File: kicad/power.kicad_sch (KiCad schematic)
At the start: 48 parts, among them J5 Conn_Coaxial_Power, J6 Screw_Terminal_01x02, U11 ADP7118ACPZN, U22 ADP7118ACPZN, U23 LTM8074EY-PBF, U7 LTM8078EY-PBF, U8 ADP7118ACPZN, U9 ADP7118ACPZN

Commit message: assign footprints
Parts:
- C15, C69, C7: footprint (none) -> Capacitor_SMD:C_0805_2012Metric_Pad1.18x1.45mm_HandSolder
- C16, C17, C18, C19, C20, C21, C26, C27, C28, C65, C66, C67, C68, C70, C71, C72, C8: footprint (none) -> Capacitor_SMD:C_0603_1608Metric_Pad1.08x0.95mm_HandSolder
- F1: footprint (none) -> Fuse:Fuse_2920_7451Metric_Pad2.10x5.45mm_HandSolder
- J5: footprint (none) -> Connector_BarrelJack:BarrelJack_CUI_PJ-063AH_Horizontal
- J6: footprint (none) -> TerminalBlock_Phoenix:TerminalBlock_Phoenix_MKDS-1,5-2_1x02_P5.00mm_Horizontal
- R12, R19, R21, R22, R65, R66, R67, R68, R69, R70, R71, R72, R73, R74, R75, R76, R77, R91, R92: footprint (none) -> Resistor_SMD:R_0603_1608Metric_Pad0.98x0.95mm_HandSolder
- U23: footprint 05-08-1566_ADI -> bgelb_footprint:05-08-1566_ADI
- U7: footprint LTM8078IY-PBF_ADI -> bgelb_footprint:LTM8078IY-PBF_ADI

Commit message: fix ercs
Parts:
- U23: footprint bgelb_footprint:05-08-1566_ADI -> 05-08-1566_ADI
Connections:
- net GND: now also U23.A1 (GND), U23.A5 (GND), U23.B2 (GND), U23.B3 (GND), U23.B4 (GND), U23.C2 (GND), U23.C3 (GND), U23.C4 (GND), U23.C5 (GND), U23.D2 (GND), U23.D3 (GND), U23.D4 (GND), U23.E3 (GND), U23.E4 (GND), U23.E5 (GND)

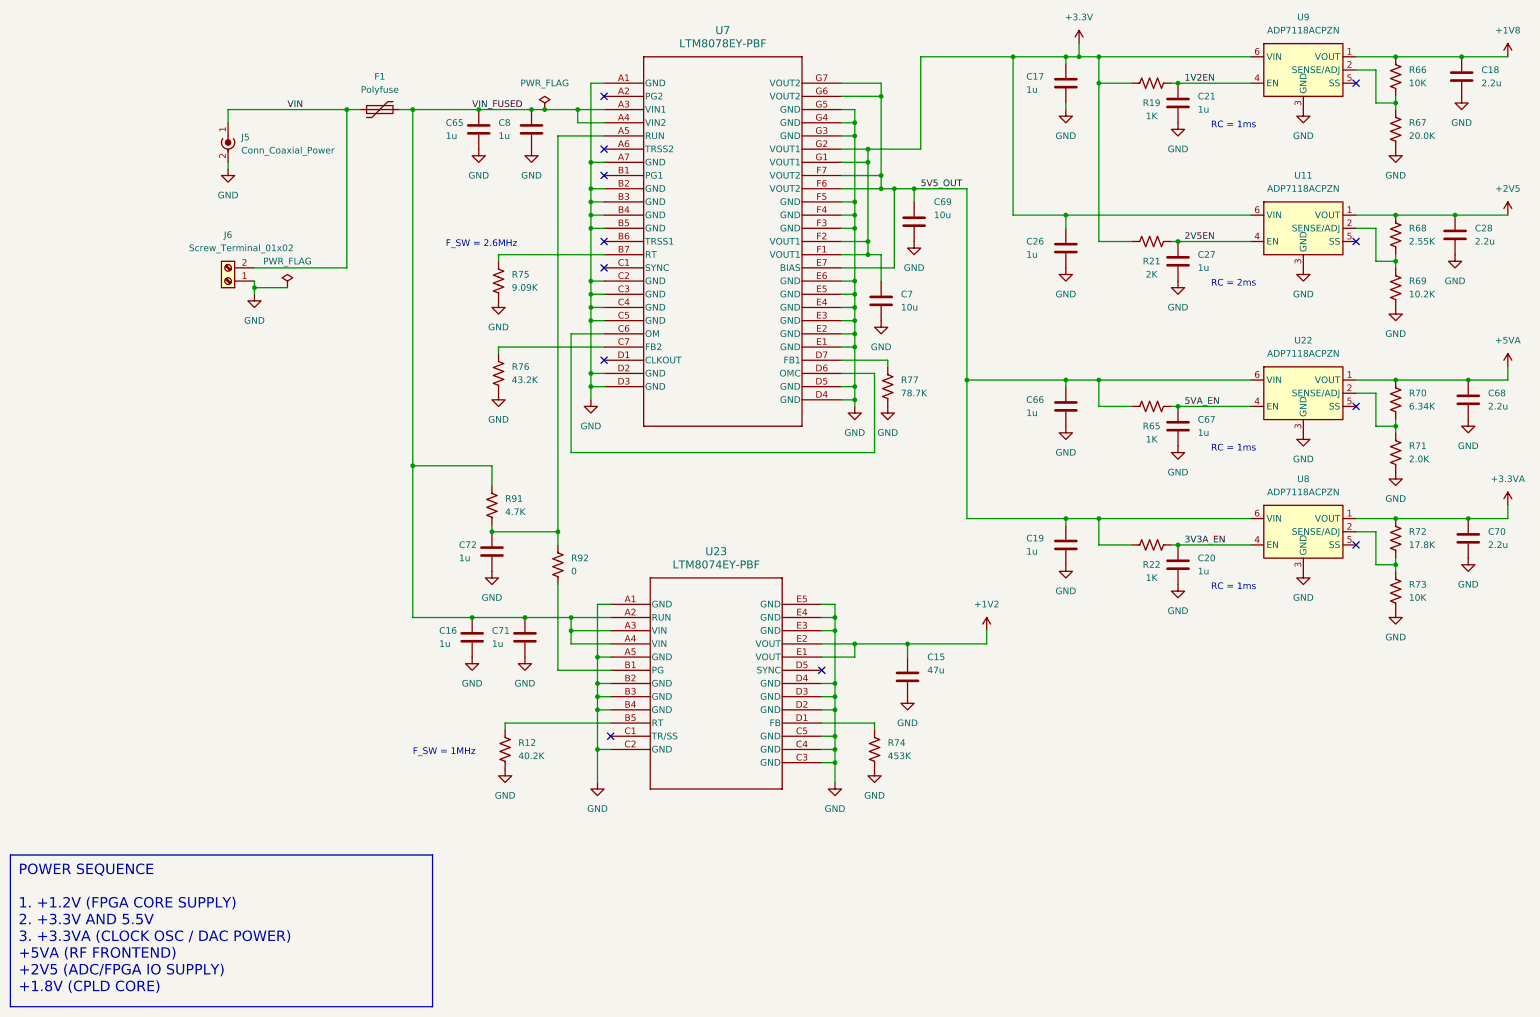
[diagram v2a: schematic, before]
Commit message: add net names
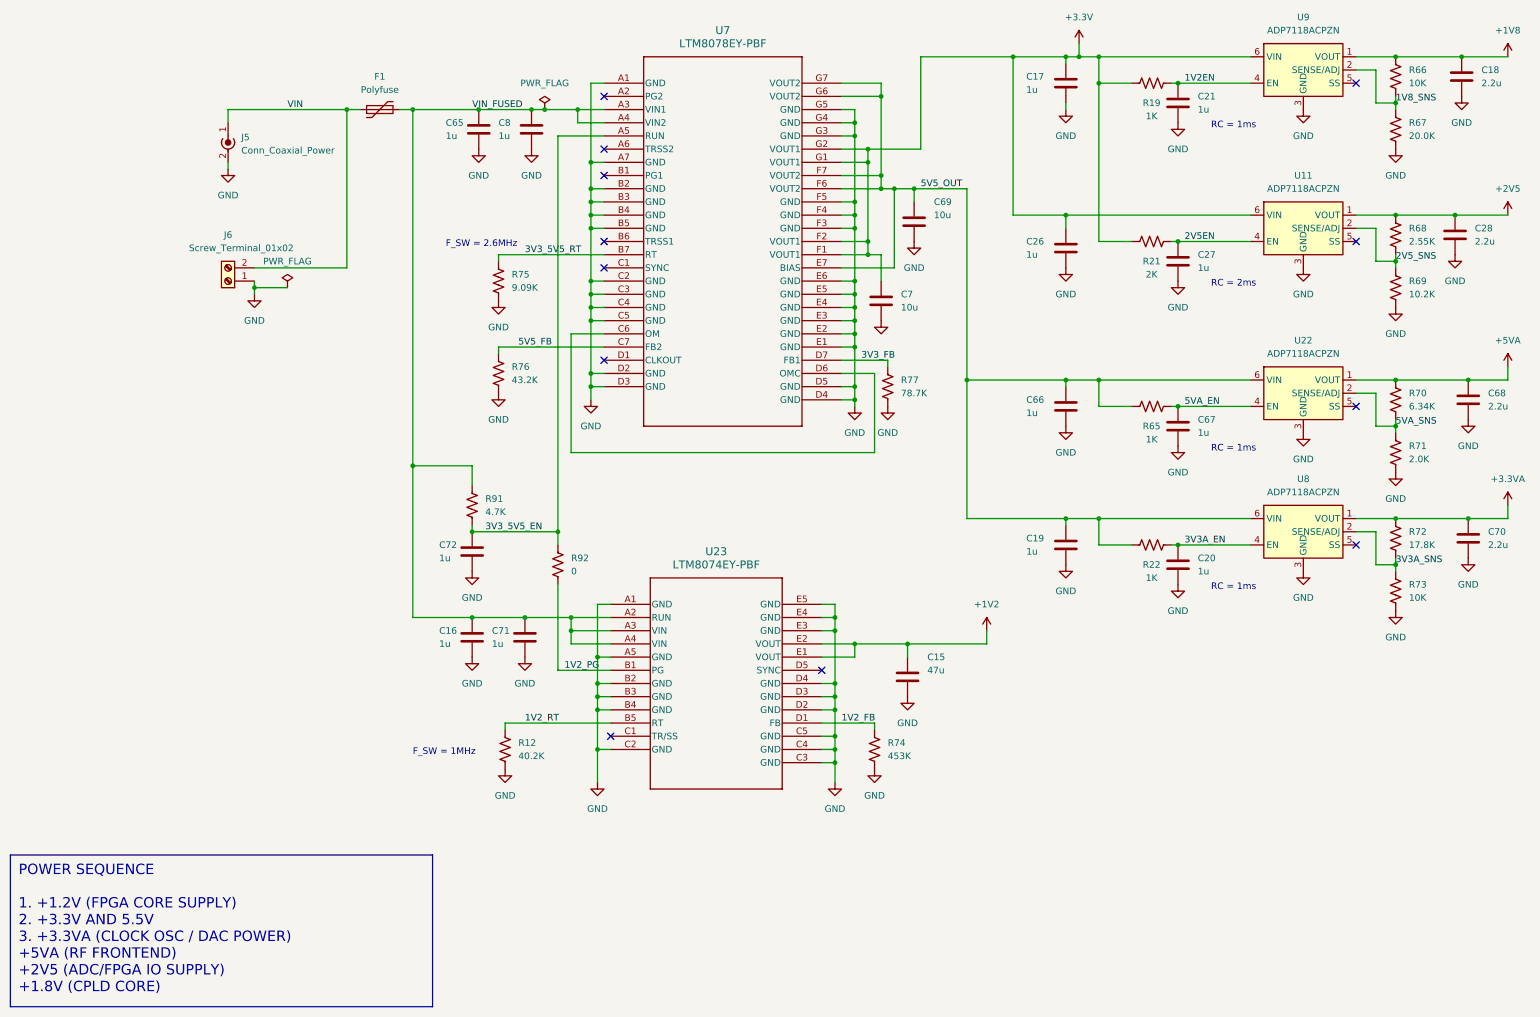
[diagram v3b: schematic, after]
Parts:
- U23: footprint 05-08-1566_ADI -> bgelb_footprint:05-08-1566_ADI
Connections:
- net 3V3_5V5_EN: now reaches C72.1, R91.2, R92.1, U7.A5 (RUN)
- net 1V8_SNS: now reaches R66.2, R67.1, U9.2 (SENSE/ADJ)
- net 3V3A_SNS: now reaches R72.2, R73.1, U8.2 (SENSE/ADJ)
- net 2V5_SNS: now reaches R68.2, R69.1, U11.2 (SENSE/ADJ)
- net 5VA_SNS: now reaches R70.2, R71.1, U22.2 (SENSE/ADJ)
- net 5V5_FB: now reaches R76.1, U7.C7 (FB2)
- net 3V3_5V5_RT: now reaches R75.1, U7.B7 (RT)
- net 3V3_FB: now reaches R77.1, U7.D7 (FB1)
- net 1V2_PG: now reaches R92.2, U23.B1 (PG)
- net 1V2_RT: now reaches R12.1, U23.B5 (RT)
- net 1V2_FB: now reaches R74.1, U23.D1 (FB)
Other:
- moved on the sheet: C72, R91
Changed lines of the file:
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@@
   (junction (at 246.38 57.15) (diameter 0) (color 0 0 0 0)
   )
-  (junction (at 146.05 148.59) (diameter 0) (color 0 0 0 0)
+  (junction (at 142.24 148.59) (diameter 0) (color 0 0 0 0)
   )
   (junction (at 334.01 119.38) (diameter 0) (color 0 0 0 0)
@@
     (stroke (width 0) (type default))
   )
+  (wire (pts (xy 142.24 148.59) (xy 158.75 148.59))
+    (stroke (width 0) (type default))
+  )
   (wire (pts (xy 213.36 72.39) (xy 215.9 72.39))
     (stroke (width 0) (type default))
@@
     (stroke (width 0) (type default))
   )
-  (wire (pts (xy 146.05 139.7) (xy 146.05 135.89))
+  (wire (pts (xy 142.24 139.7) (xy 142.24 135.89))
     (stroke (width 0) (type default))
   )
@@
     (stroke (width 0) (type default))
   )
-  (wire (pts (xy 146.05 148.59) (xy 158.75 148.59))
-    (stroke (width 0) (type default))
-  )
-  (wire (pts (xy 146.05 135.89) (xy 130.81 135.89))
+  (wire (pts (xy 142.24 135.89) (xy 130.81 135.89))
     (stroke (width 0) (type default))
   )
@@
     (stroke (width 0) (type default))
   )
-  (wire (pts (xy 146.05 147.32) (xy 146.05 148.59))
+  (wire (pts (xy 142.24 147.32) (xy 142.24 148.59))
     (stroke (width 0) (type default))
   )
@@
     (effects (font (size 1.27 1.27)) (justify left bottom))
   )
+  (label "1V2_PG" (at 160.02 175.26 0) (fields_autoplaced)
+    (effects (font (size 1.27 1.27)) (justify left bottom))
+  )
   (label "VIN_FUSED" (at 142.24 67.31 0) (fields_autoplaced)
     (effects (font (size 1.27 1.27)) (justify left bottom))
   )
+  (label "1V8_SNS" (at 320.04 66.04 0) (fields_autoplaced)
+    (effects (font (size 1.27 1.27)) (justify left bottom))
+  )
+  (label "1V2_RT" (at 152.4 185.42 0) (fields_autoplaced)
+    (effects (font (size 1.27 1.27)) (justify left bottom))
+  )
+  (label "3V3_FB" (at 217.17 115.57 0) (fields_autoplaced)
+    (effects (font (size 1.27 1.27)) (justify left bottom))
+  )
+  (label "5V5_FB" (at 151.13 113.03 0) (fields_autoplaced)
+    (effects (font (size 1.27 1.27)) (justify left bottom))
+  )
   (label "1V2EN" (at 279.4 62.23 0) (fields_autoplaced)
     (effects (font (size 1.27 1.27)) (justify left bottom))
@@
     (effects (font (size 1.27 1.27)) (justify left bottom))
   )
+  (label "3V3_5V5_RT" (at 152.4 95.25 0) (fields_autoplaced)
+    (effects (font (size 1.27 1.27)) (justify left bottom))
+  )
+  (label "1V2_FB" (at 213.36 185.42 0) (fields_autoplaced)
+    (effects (font (size 1.27 1.27)) (justify left bottom))
+  )
+  (label "3V3A_SNS" (at 320.04 154.94 0) (fields_autoplaced)
+    (effects (font (size 1.27 1.27)) (justify left bottom))
+  )
   (label "VIN" (at 106.68 67.31 0) (fields_autoplaced)
     (effects (font (size 1.27 1.27)) (justify left bottom))
   )
+  (label "5VA_SNS" (at 320.04 128.27 0) (fields_autoplaced)
+    (effects (font (size 1.27 1.27)) (justify left bottom))
+  )
   (label "3V3A_EN" (at 279.4 151.13 0) (fields_autoplaced)
+    (effects (font (size 1.27 1.27)) (justify left bottom))
+  )
+  (label "3V3_5V5_EN" (at 144.78 148.59 0) (fields_autoplaced)
+    (effects (font (size 1.27 1.27)) (justify left bottom))
+  )
+  (label "2V5_SNS" (at 320.04 96.52 0) (fields_autoplaced)
     (effects (font (size 1.27 1.27)) (justify left bottom))
   )
@@
     )
   )
-  (symbol (lib_id "Device:C") (at 146.05 152.4 0) (unit 1)
+  (symbol (lib_id "Device:C") (at 142.24 152.4 0) (unit 1)
     (in_bom yes) (on_board yes) (dnp no)
-    (property "Reference" "C72" (at 139.7 151.13 0)
-      (effects (font (size 1.27 1.27)) (justify left))
-    )
-    (property "Value" "1u" (at 139.7 153.67 0)
-      (effects (font (size 1.27 1.27)) (justify left))
-    )
-    (property "Footprint" "Capacitor_SMD:C_0603_1608Metric_Pad1.08x0.95mm_HandSolder" (at 147.0152 156.21 0)
-      (effects (font (size 1.27 1.27)) hide)
-    )
-    (property "Datasheet" "~" (at 146.05 152.4 0)
+    (property "Reference" "C72" (at 135.89 151.13 0)
+      (effects (font (size 1.27 1.27)) (justify left))
+    )
+    (property "Value" "1u" (at 135.89 153.67 0)
+      (effects (font (size 1.27 1.27)) (justify left))
+    )
+    (property "Footprint" "Capacitor_SMD:C_0603_1608Metric_Pad1.08x0.95mm_HandSolder" (at 143.2052 156.21 0)
+      (effects (font (size 1.27 1.27)) hide)
+    )
+    (property "Datasheet" "~" (at 142.24 152.4 0)
       (effects (font (size 1.27 1.27)) hide)
     )
@@
     )
   )
-  (symbol (lib_id "Device:R_US") (at 146.05 143.51 0) (unit 1)
-    (in_bom yes) (on_board yes) (dnp no) (fields_autoplaced)
-    (property "Reference" "R91" (at 148.59 142.24 0)
-      (effects (font (size 1.27 1.27)) (justify left))
-    )
-    (property "Value" "4.7K" (at 148.59 144.78 0)
-      (effects (font (size 1.27 1.27)) (justify left))
-    )
-    (property "Footprint" "Resistor_SMD:R_0603_1608Metric_Pad0.98x0.95mm_HandSolder" (at 147.066 143.764 90)
-      (effects (font (size 1.27 1.27)) hide)
-    )
-    (property "Datasheet" "~" (at 146.05 143.51 0)
+  (symbol (lib_id "Device:R_US") (at 142.24 143.51 0) (unit 1)
+    (in_bom yes) (on_board yes) (dnp no) (fields_autoplaced)
+    (property "Reference" "R91" (at 144.78 142.24 0)
+      (effects (font (size 1.27 1.27)) (justify left))
+    )
+    (property "Value" "4.7K" (at 144.78 144.78 0)
+      (effects (font (size 1.27 1.27)) (justify left))
+    )
+    (property "Footprint" "Resistor_SMD:R_0603_1608Metric_Pad0.98x0.95mm_HandSolder" (at 143.256 143.764 90)
+      (effects (font (size 1.27 1.27)) hide)
+    )
+    (property "Datasheet" "~" (at 142.24 143.51 0)
       (effects (font (size 1.27 1.27)) hide)
     )
@@
     )
     (property "Value" "GND" (at 220.98 113.03 0)
-      (effects (font (size 1.27 1.27)))
+      (effects (font (size 1.27 1.27)) hide)
     )
     (property "Footprint" "" (at 220.98 107.95 0)
@@
       (effects (font (size 1.524 1.524)))
     )
-    (property "Footprint" "05-08-1566_ADI" (at 168.91 162.56 0)
+    (property "Footprint" "bgelb_footprint:05-08-1566_ADI" (at 168.91 162.56 0)
       (effects (font (size 1.27 1.27) italic) hide)
     )
@@
     )
   )
-  (symbol (lib_id "power:GND") (at 146.05 156.21 0) (unit 1)
-    (in_bom yes) (on_board yes) (dnp no) (fields_autoplaced)
-    (property "Reference" "#PWR0151" (at 146.05 162.56 0)
-      (effects (font (size 1.27 1.27)) hide)
-    )
-    (property "Value" "GND" (at 146.05 161.29 0)
-      (effects (font (size 1.27 1.27)))
-    )
-    (property "Footprint" "" (at 146.05 156.21 0)
-      (effects (font (size 1.27 1.27)) hide)
-    )
-    (property "Datasheet" "" (at 146.05 156.21 0)
-      (effects (font (size 1.27 1.27)) hide)
-    )
+  (symbol (lib_id "power:GND") (at 142.24 156.21 0) (unit 1)
+    (in_bom yes) (on_board yes) (dnp no) (fields_autoplaced)
+    (property "Reference" "#PWR0151" (at 142.24 162.56 0)
+      (effects (font (size 1.27 1.27)) hide)
+    )
+    (property "Value" "GND" (at 142.24 161.29 0)
+      (effects (font (size 1.27 1.27)))
+    )
+    (property "Footprint" "" (at 142.24 156.21 0)
+      (effects (font (size 1.27 1.27)) hide)
+    )
+    (property "Datasheet" "" (at 142.24 156.21 0)
+      (effects (font (size 1.27 1.27)) hide)
+    )
